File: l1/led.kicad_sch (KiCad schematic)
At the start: 30 parts

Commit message: rough ideation
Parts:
- removed D10, D11, D12, D13, D14, D15, D16, D17, D18, D19, D20, D21, D22, D23, D24, D25, D26, D27, D28, D29, D30, D31, D32, D33, D4, D5, D6, D7, D8, D9: LED, Library:led2835, symbol Device:LED
- added D201, D202, D203, D204, D205, D206, D207, D208, D209, D210, D211, D212, D213, D214, D215, D216, D217, D218, D219, D220, D221, D222, D223, D224, D225, D226, D227, D228, D229, D230: LED, Library:led2835, symbol Device:LED
- added R235, R236, R237, R238, R239, R240, R241, R242, R243, R244, R245, R246, R247, R248, R249, R250, R251, R252, R253, R254, R255, R256, R257, R258, R259, R260, R261, R262, R263, R264: R, Library:res0603, symbol Device:R
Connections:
- net +3V3: now also D201.2 (A), D202.2 (A), D203.2 (A), D204.2 (A), D205.2 (A), D206.2 (A), D207.2 (A), D208.2 (A), D209.2 (A), D210.2 (A), D211.2 (A), D212.2 (A), D213.2 (A), D214.2 (A), D215.2 (A), D216.2 (A), D217.2 (A), D218.2 (A), D219.2 (A), D220.2 (A), D221.2 (A), D222.2 (A), D223.2 (A), D224.2 (A), D225.2 (A), D226.2 (A), D227.2 (A), D228.2 (A), D229.2 (A), D230.2 (A)
- new net: D212.1 (K), R246.1
- new net: D229.1 (K), R263.1
- new net: D215.1 (K), R249.1
- new net: D209.1 (K), R243.1
- new net: D202.1 (K), R236.1
- new net: D221.1 (K), R255.1
- new net: D218.1 (K), R252.1
- new net: D230.1 (K), R264.1
- new net: D216.1 (K), R250.1
- new net: D214.1 (K), R248.1
- new net: D225.1 (K), R259.1
- new net: D207.1 (K), R241.1
- new net: D226.1 (K), R260.1
- new net: D224.1 (K), R258.1
- new net: D223.1 (K), R257.1
- new net: D204.1 (K), R238.1
- new net: D206.1 (K), R240.1
- new net: D211.1 (K), R245.1
- new net: D217.1 (K), R251.1
- new net: D227.1 (K), R261.1
- new net: D201.1 (K), R235.1
- new net: D219.1 (K), R253.1
- new net: D222.1 (K), R256.1
- new net: D210.1 (K), R244.1
- new net: D220.1 (K), R254.1
- new net: D208.1 (K), R242.1
- new net: D203.1 (K), R237.1
- new net: D213.1 (K), R247.1
- new net: D205.1 (K), R239.1
- new net: D228.1 (K), R262.1
- new net GNDREF: R235.2, R236.2, R237.2, R238.2, R239.2, R240.2, R241.2, R242.2, R243.2, R244.2, R245.2, R246.2, R247.2, R248.2, R249.2, R250.2, R251.2, R252.2, R253.2, R254.2, R255.2, R256.2, R257.2, R258.2, R259.2, R260.2, R261.2, R262.2, R263.2, R264.2

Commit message: 死
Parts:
- removed D201, D202, D203, D204, D205, D206, D207, D208, D209, D210, D211, D212, D213, D214, D215, D216, D217, D218, D219, D220, D221, D222, D223, D224, D225, D226, D227, D228, D229, D230: LED, Library:led2835, symbol Device:LED
- removed R235, R236, R237, R238, R239, R240, R241, R242, R243, R244, R245, R246, R247, R248, R249, R250, R251, R252, R253, R254, R255, R256, R257, R258, R259, R260, R261, R262, R263, R264: R, Library:res0603, symbol Device:R
- added C? (x2): 22u, symbol Device:C
- added C? (x3): 0u1, symbol Device:C
- added C?: 10n, symbol Device:C
- added C?: 1u, symbol Device:C
- added C?: 10u, symbol Device:C
- added D? (x30): LED, Library:led2835, symbol Device:LED
- added D?: 1N5819, symbol Device:D_Schottky
- added L?: 120u, symbol Device:L
- added R?: 10K, symbol Device:R
- added R?: 1, symbol Device:R
- added R?: R, symbol Device:R
- added R? (x10): 150, Library:res0603, symbol Device:R
- added R?: 100K, symbol Device:R
- added R?: 0.3, symbol Device:R
- added SW?: SW_SPDT, symbol Switch:SW_SPDT
- added U?: TPS22917x, symbol vincent:TPS22917x
- added U?: ILD8150, symbol vincent:ILD8150
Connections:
- new net: D?.1 (K), D?.2 (A) (x20)
- new net: D?.1 (K), R?.1 (x10)
- new net: R?.1, R?.2, SW?.2 (B)
- new net: R?.1, R?.2
- new net: C?.1, R?.1, U?. (VOUT), U?.8 (VIN)
- new net: C?.2, D?.1 (K), L?.1, U?.1 (SW)
- new net: C?.1, U?.2 (BOOT)
- new net: C?.2, U?. (VOUT)
- new net: R?.2, U?. (VOUT)
- new net: C?.1, U?.7 (VCC)
- new net +12V: C?.1, C?.1, C?.1, U?. (VOUT)
- new net +3V3 FLIT: R?.1
- new net EP: C?.2, C?.2, C?.2, C?.2, C?.2, D?.2 (A), R?.2, SW?.1 (A), U?.4 (GND), U?.9 (EP)
- new net LED DIM: U?.3 (DIM)
- new net LED PWR: C?.1, R?.2, U?. (VOUT)
- new net LED VIN: C?.1, D?.2 (A), D?.2 (A), D?.2 (A), D?.2 (A), D?.2 (A), D?.2 (A), D?.2 (A), D?.2 (A), D?.2 (A), D?.2 (A), L?.2
- new net LED VOUT: C?.2, R?.1, R?.2, R?.2, R?.2, R?.2, R?.2, R?.2, R?.2, R?.2, R?.2, R?.2, U?.5 (CS)
- no-connect marks 0 -> 2

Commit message: 死
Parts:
- C211, C212, C213, C214, C215, C216, C217, C218: renamed from C?; footprint (none) -> Library:cap0603
- R247, R248, R249, R250, R251: renamed from R?; footprint (none) -> Library:res0603
- SW201: renamed from SW?; footprint (none) -> Library:SS12D00G3
- U204: renamed from U?; footprint (none) -> Library:SOT-23-6
- U205: renamed from U?; footprint (none) -> Package_SO:Infineon_PG-DSO-8-27_3.9x4.9mm_EP2.65x3mm_ThermalVias
- gave numbers to parts that had none: 42
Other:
- moved on the sheet: C211, C212, C213, C214, C215, C216, C217, C218, D232, L201, R247, R248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

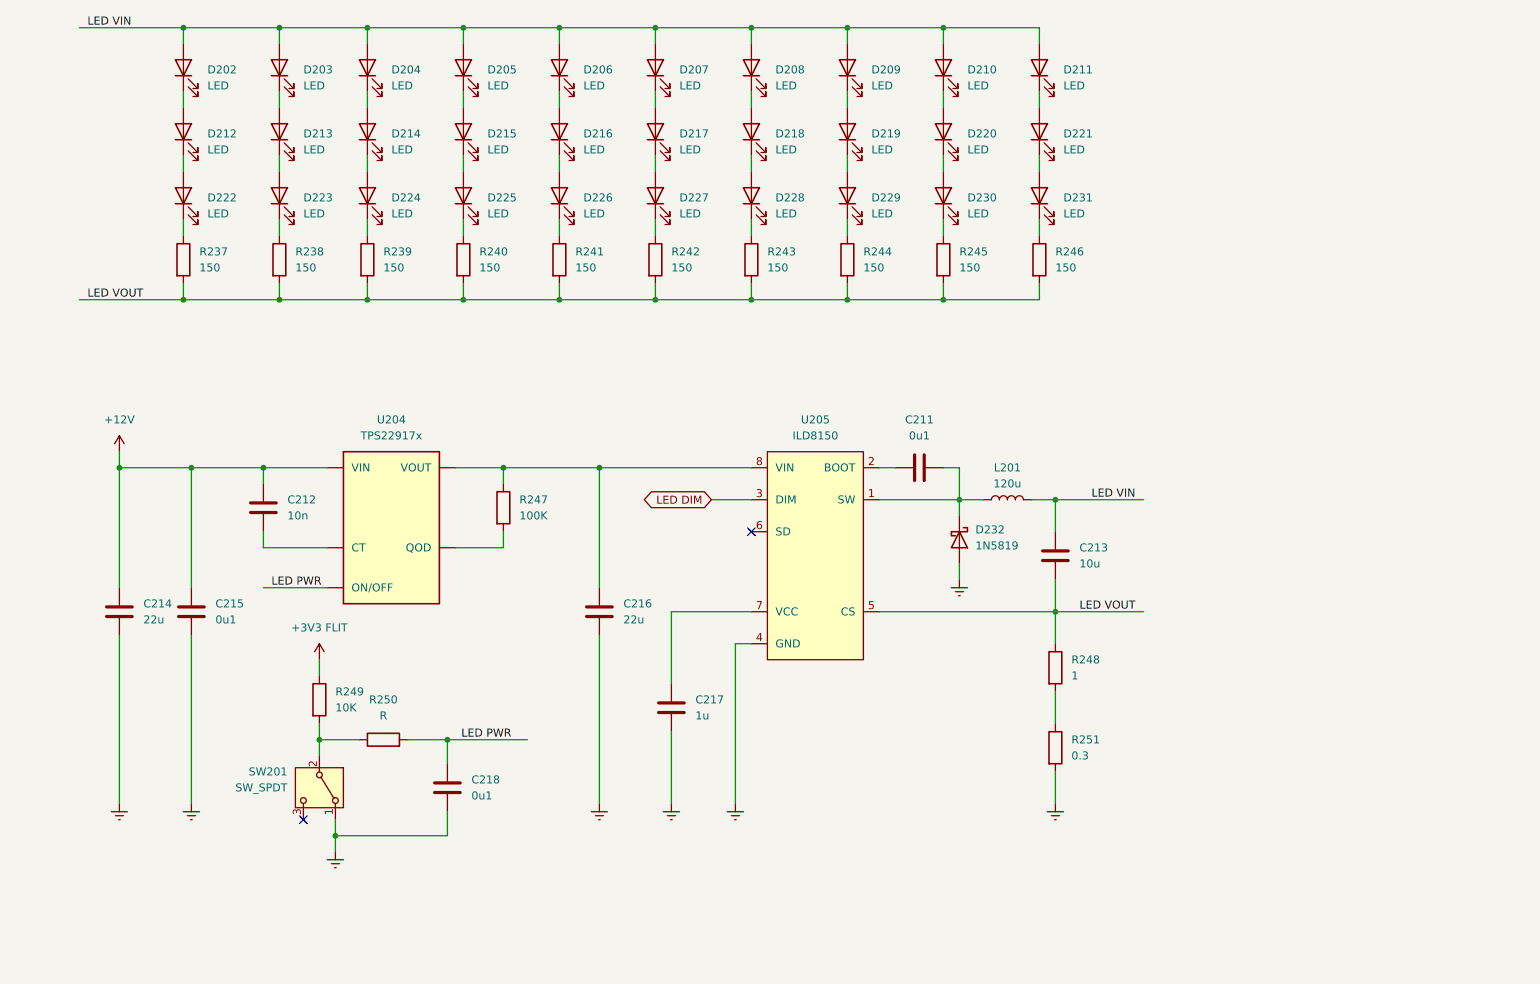
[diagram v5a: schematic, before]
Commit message: Going to move to VNH
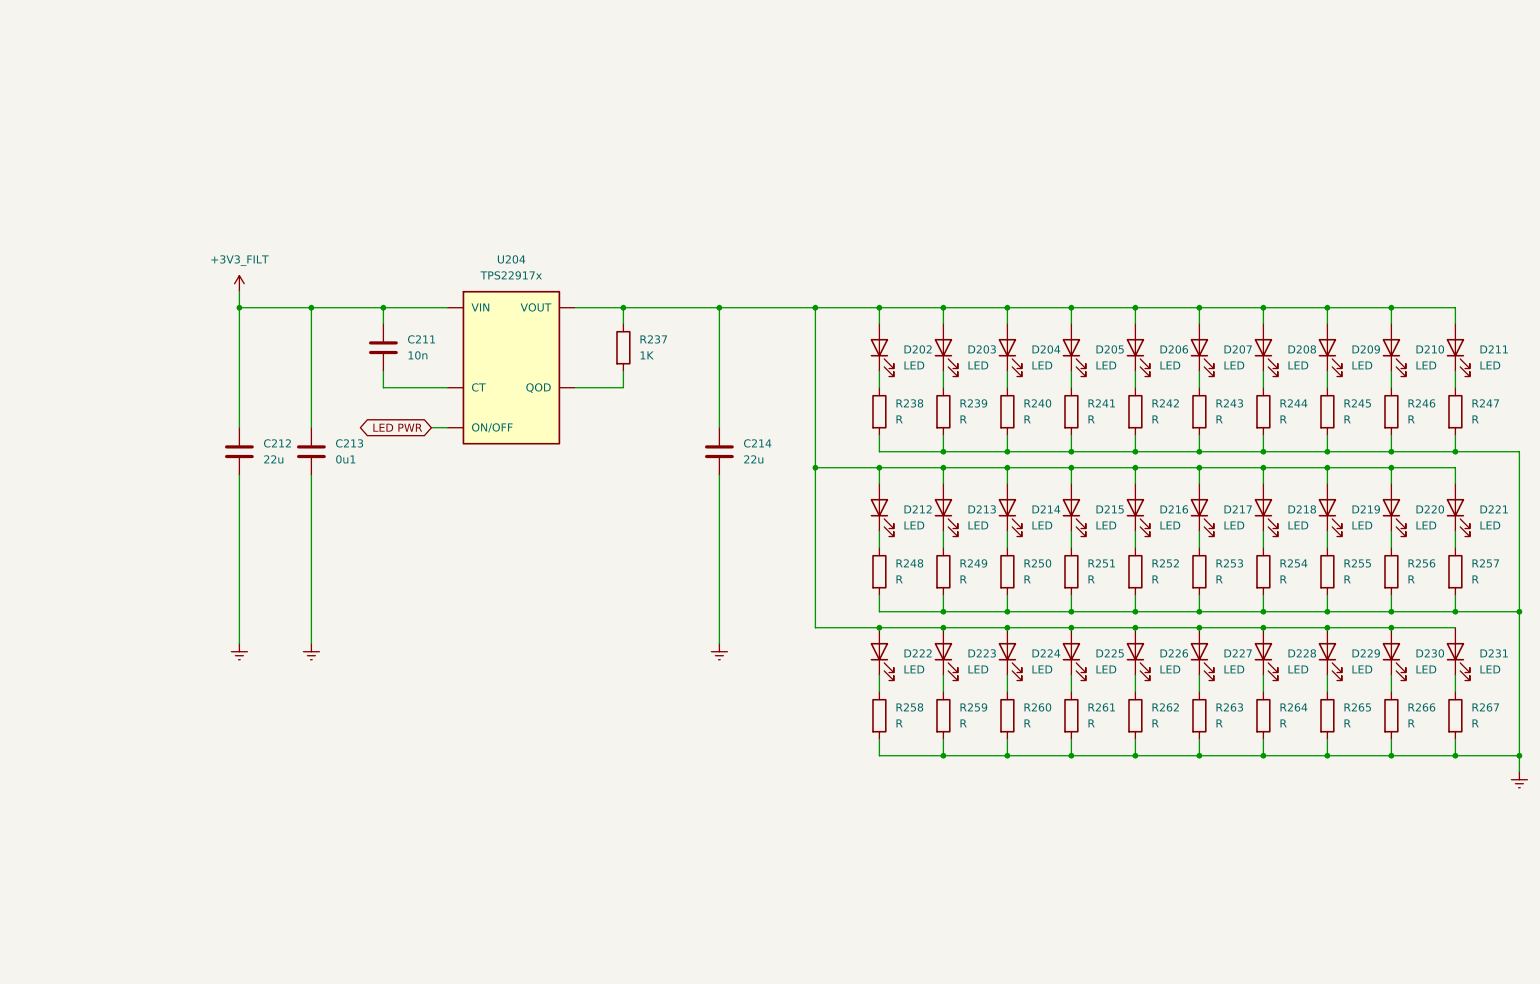
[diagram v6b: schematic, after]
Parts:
- removed C211, C218: 0u1, Library:cap0603, symbol Device:C
- removed C213: 10u, Library:cap0603, symbol Device:C
- removed C217: 1u, Library:cap0603, symbol Device:C
- removed D232: 1N5819, symbol Device:D_Schottky
- removed L201: 120u, symbol Device:L
- removed R237: 150, Library:res0603, symbol Device:R
- removed SW201: SW_SPDT, Library:SS12D00G3, symbol Switch:SW_SPDT
- removed U205: ILD8150, Package_SO:Infineon_PG-DSO-8-27_3.9x4.9mm_EP2.65x3mm_ThermalVias, symbol vincent:ILD8150
- added R247, R252, R253, R254, R255, R256, R257, R258, R259, R260, R261, R262, R263, R264, R265, R266, R267: R, Library:res0603, symbol Device:R
- R237: renamed from R247; value 100K -> 1K
- R238, R239, R240, R241, R242, R243, R244, R245, R246: value 150 -> R
- R248: value 1 -> R
- R249: value 10K -> R
- R251: value 0.3 -> R
- renumbered C212 to C211, C214 to C212, C215 to C213, C216 to C214
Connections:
- net +3V3 FLIT is gone; now on an unnamed net: R249.1
- net EP is gone; now on net GNDREF: C212.2, C213.2, C214.2, R251.2
- net LED VIN is gone; now on an unnamed net: D202.2 (A), D203.2 (A), D204.2 (A), D205.2 (A), D206.2 (A), D207.2 (A), D208.2 (A), D209.2 (A), D210.2 (A), D211.2 (A)
- net LED PWR: no longer R250.2
- net at D213.2 (A): now also C214.1, D212.2 (A), D214.2 (A), D215.2 (A), D216.2 (A), D217.2 (A), D218.2 (A), D219.2 (A), D220.2 (A), D221.2 (A), D222.2 (A), D223.2 (A), D224.2 (A), D225.2 (A), D226.2 (A), D227.2 (A), D228.2 (A), D229.2 (A), D230.2 (A), D231.2 (A), R237.1, U204. (VOUT); no longer D203.1 (K)
- net at D218.1 (K): now also R254.1; no longer D228.2 (A)
- net at D208.1 (K): now also R244.1; no longer D218.2 (A)
- net at R240.1: now also D204.1 (K); no longer D225.1 (K)
- net at D215.1 (K): now also R251.1; no longer D225.2 (A)
- net at D223.1 (K): now also R259.1; no longer R238.1
- net at D213.1 (K): no longer D223.2 (A)
- net at D230.1 (K): now also R266.1; no longer R245.1
- net at D220.1 (K): now also R256.1; no longer D230.2 (A)
- net at D221.1 (K): now also R257.1; no longer D231.2 (A)
- net at D211.1 (K): now also R247.1; no longer D221.2 (A)
- net at D224.1 (K): now also R260.1; no longer R239.1
- net at D214.1 (K): now also R250.1; no longer D224.2 (A)
- net at R246.1: now also D210.1 (K); no longer D231.1 (K)
- net GNDREF: now reaches R249.2
- net GNDREF: now also R238.2, R239.2, R240.2, R241.2, R242.2, R243.2, R244.2, R245.2, R246.2, R248.2, R250.2, R247.2, R252.2, R253.2, R254.2, R255.2, R256.2, R257.2, R258.2, R259.2, R260.2, R261.2, R262.2, R263.2, R264.2, R265.2, R266.2, R267.2; no longer R250.1
- net at D226.1 (K): now also R262.1; no longer R241.1
- net at D216.1 (K): now also R252.1; no longer D226.2 (A)
- net at D205.1 (K): now also R241.1; no longer D215.2 (A)
- net at D209.1 (K): now also R245.1; no longer D219.2 (A)
- net at D228.1 (K): now also R264.1; no longer R243.1
- net at D222.1 (K): now also R258.1
- net at D229.1 (K): now also R265.1; no longer R244.1
- net at R242.1: now also D206.1 (K); no longer D227.1 (K)
- net at D219.1 (K): now also R255.1; no longer D229.2 (A)
- net at D212.1 (K): now also R248.1; no longer D222.2 (A)
- net at D217.1 (K): now also R253.1; no longer D227.2 (A)
- net at D207.1 (K): now also R243.1; no longer D217.2 (A)
- net at D202.1 (K): now also R238.1; no longer D212.2 (A)
- net +12V renamed +3V3_FILT
- removed net LED VOUT: R238.2, R239.2, R240.2, R241.2, R242.2, R243.2, R244.2, R245.2, R246.2, R248.1
- new net: D225.1 (K), R261.1
- new net: D203.1 (K), R239.1
- new net: D231.1 (K), R267.1
- new net: D227.1 (K), R263.1
- no-connect marks 2 -> 0
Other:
- moved on the sheet: C211, C212, C213, C214, R237, U204

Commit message: L1 - Left wiring
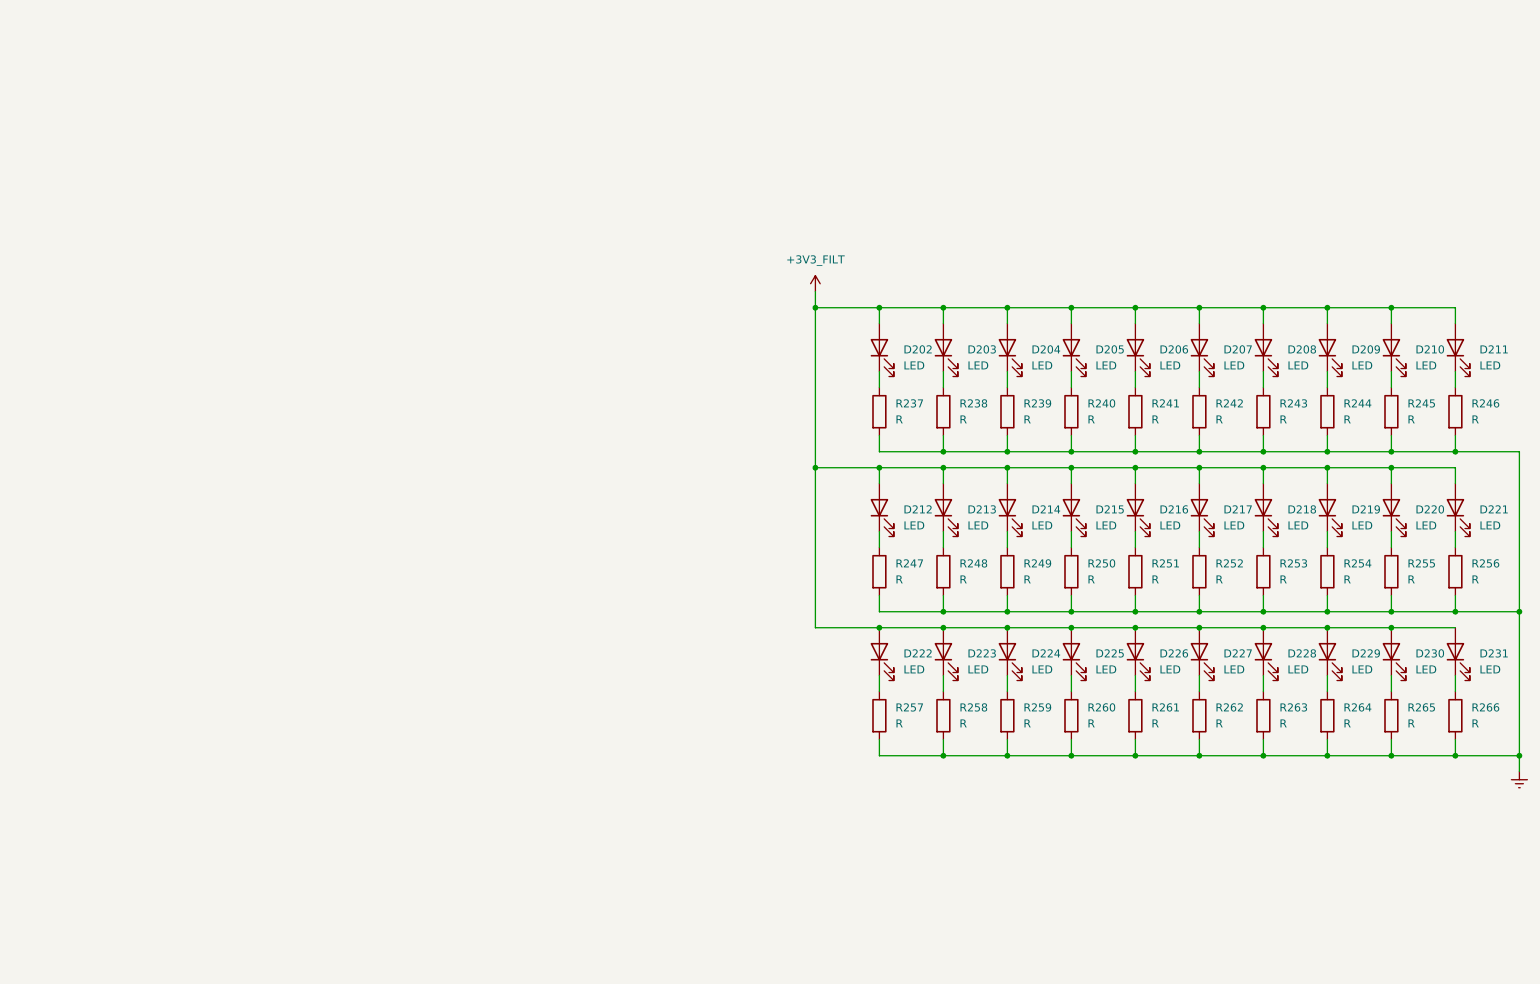
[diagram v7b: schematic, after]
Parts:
- removed C211: 10n, Library:cap0603, symbol Device:C
- removed C212, C214: 22u, Library:cap0603, symbol Device:C
- removed C213: 0u1, Library:cap0603, symbol Device:C
- removed R237: 1K, Library:res0603, symbol Device:R
- removed U204: TPS22917x, Library:SOT-23-6, symbol vincent:TPS22917x
- renumbered R238 to R237, R239 to R238, R240 to R239, R241 to R240, R242 to R241, R243 to R242, R244 to R243, R245 to R244, R246 to R245, R247 to R246, R248 to R247, R249 to R248, R250 to R249, R251 to R250, R252 to R251, R253 to R252, R254 to R253, R255 to R254, R256 to R255, R257 to R256, R258 to R257, R259 to R258, R260 to R259, R261 to R260, R262 to R261, R263 to R262, R264 to R263, R265 to R264, R266 to R265, R267 to R266
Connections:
- net +3V3_FILT: now also D202.2 (A), D203.2 (A), D204.2 (A), D205.2 (A), D206.2 (A), D207.2 (A), D208.2 (A), D209.2 (A), D210.2 (A), D211.2 (A), D212.2 (A), D213.2 (A), D214.2 (A), D215.2 (A), D216.2 (A), D217.2 (A), D218.2 (A), D219.2 (A), D220.2 (A), D221.2 (A), D222.2 (A), D223.2 (A), D224.2 (A), D225.2 (A), D226.2 (A), D227.2 (A), D228.2 (A), D229.2 (A), D230.2 (A), D231.2 (A)

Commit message: l1 temp
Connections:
- net +3V3_FILT renamed +3V3
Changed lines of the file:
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@@
+	)
+	(symbol
+		(lib_id "power:+3V3")
+		(at 143.51 67.31 0)
+		(unit 1)
+		(exclude_from_sim no)
+		(in_bom yes)
+		(on_board yes)
+		(dnp no)
+		(fields_autoplaced yes)
+		(property "Reference" "#PWR0225"
+			(at 143.51 71.12 0)
+			(effects
+				(font
+					(size 1.27 1.27)
+				)
+				(hide yes)
+			)
+		)
+		(property "Value" "+3V3"
+			(at 143.51 62.5558 0)
+			(effects
+				(font
+					(size 1.27 1.27)
+				)
+			)
+		)
+		(property "Footprint" ""
+			(at 143.51 67.31 0)
+			(effects
+				(font
+					(size 1.27 1.27)
+				)
+				(hide yes)
+			)
+		)
+		(property "Datasheet" ""
+			(at 143.51 67.31 0)
+			(effects
+				(font
+					(size 1.27 1.27)
+				)
+				(hide yes)
+			)
+		)
+		(property "Description" "Power symbol creates a global label with name \"+3V3\""
+			(at 143.51 67.31 0)
+			(effects
+				(font
+					(size 1.27 1.27)
+				)
+				(hide yes)
+			)
+		)
+		(pin "1"
+		)
+		(instances
+			(project "l1"
+				(path "/0e4ddce5-5c0a-41d1-ab67-e7bad6d98362/a63fbca6-593f-4a72-9162-84fa58a2299a/6da727bb-53e9-4f90-ad87-a0bcbe81e2aa"
+					(reference "#PWR0225")
+					(unit 1)
+				)
+			)
+		)
 	)
 	(symbol
@@
 					(unit 1)
 				)
-			)
-		)
-	)
-	(symbol
-		(lib_id "power:+3V3")
-		(at 143.51 67.31 0)
-		(unit 1)
-		(exclude_from_sim no)
-		(in_bom yes)
-		(on_board yes)
-		(dnp no)
-		(fields_autoplaced yes)
-		(property "Reference" "#PWR0225"
-			(at 143.51 71.12 0)
-			(effects
-				(font
-					(size 1.27 1.27)
-				)
-				(hide yes)
-			)
-		)
-		(property "Value" "+3V3_FILT"
-			(at 143.51 62.23 0)
-			(effects
-				(font
-					(size 1.27 1.27)
-				)
-			)
-		)
-		(property "Footprint" ""
-			(at 143.51 67.31 0)
-			(effects
-				(font
-					(size 1.27 1.27)
-				)
-				(hide yes)
-			)
-		)
-		(property "Datasheet" ""
-			(at 143.51 67.31 0)
-			(effects
-				(font
-					(size 1.27 1.27)
-				)
-				(hide yes)
-			)
-		)
-		(property "Description" "Power symbol creates a global label with name \"+3V3\""
-			(at 143.51 67.31 0)
-			(effects
-				(font
-					(size 1.27 1.27)
-				)
-				(hide yes)
-			)
-		)
-		(pin "1"
-		)
-		(instances
-			(project ""
-				(path "/0e4ddce5-5c0a-41d1-ab67-e7bad6d98362/a63fbca6-593f-4a72-9162-84fa58a2299a/6da727bb-53e9-4f90-ad87-a0bcbe81e2aa"
-					(reference "#PWR0225")
-					(unit 1)
-				)
